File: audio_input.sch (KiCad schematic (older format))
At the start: 21 parts, among them U8 OPA1664

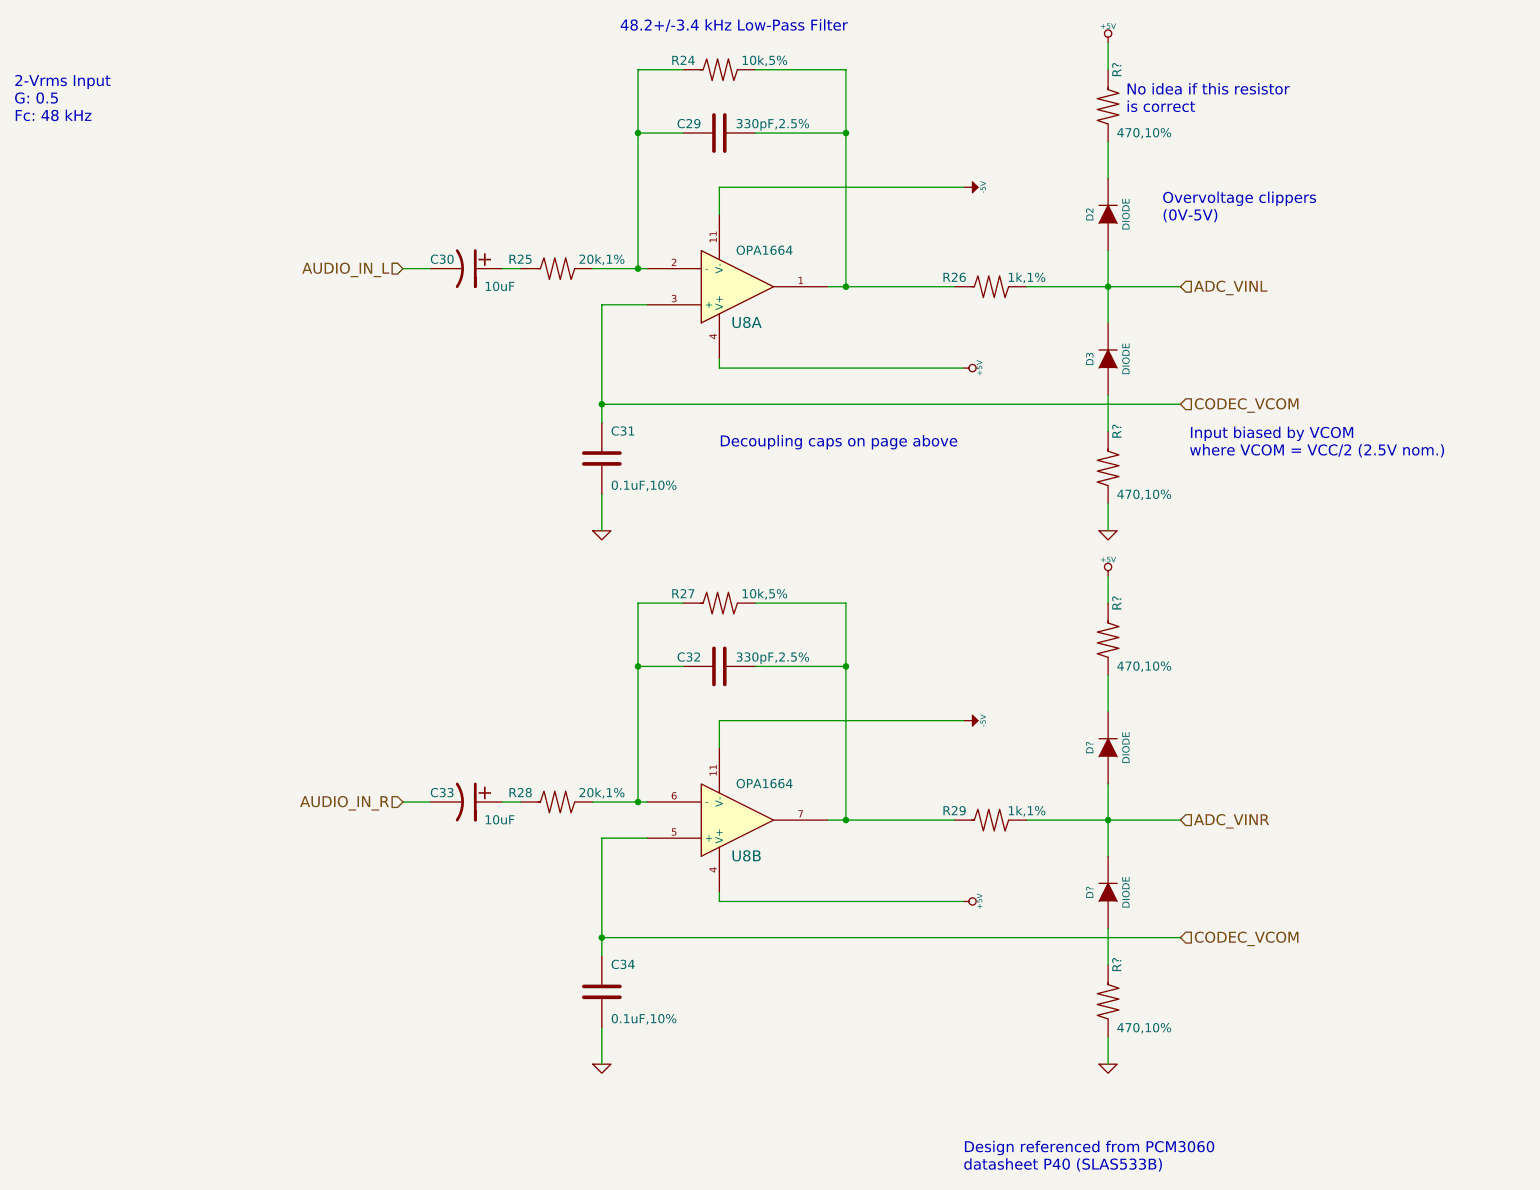
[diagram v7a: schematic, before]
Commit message: Added more footprint assoc. & eth. pulldown resistors
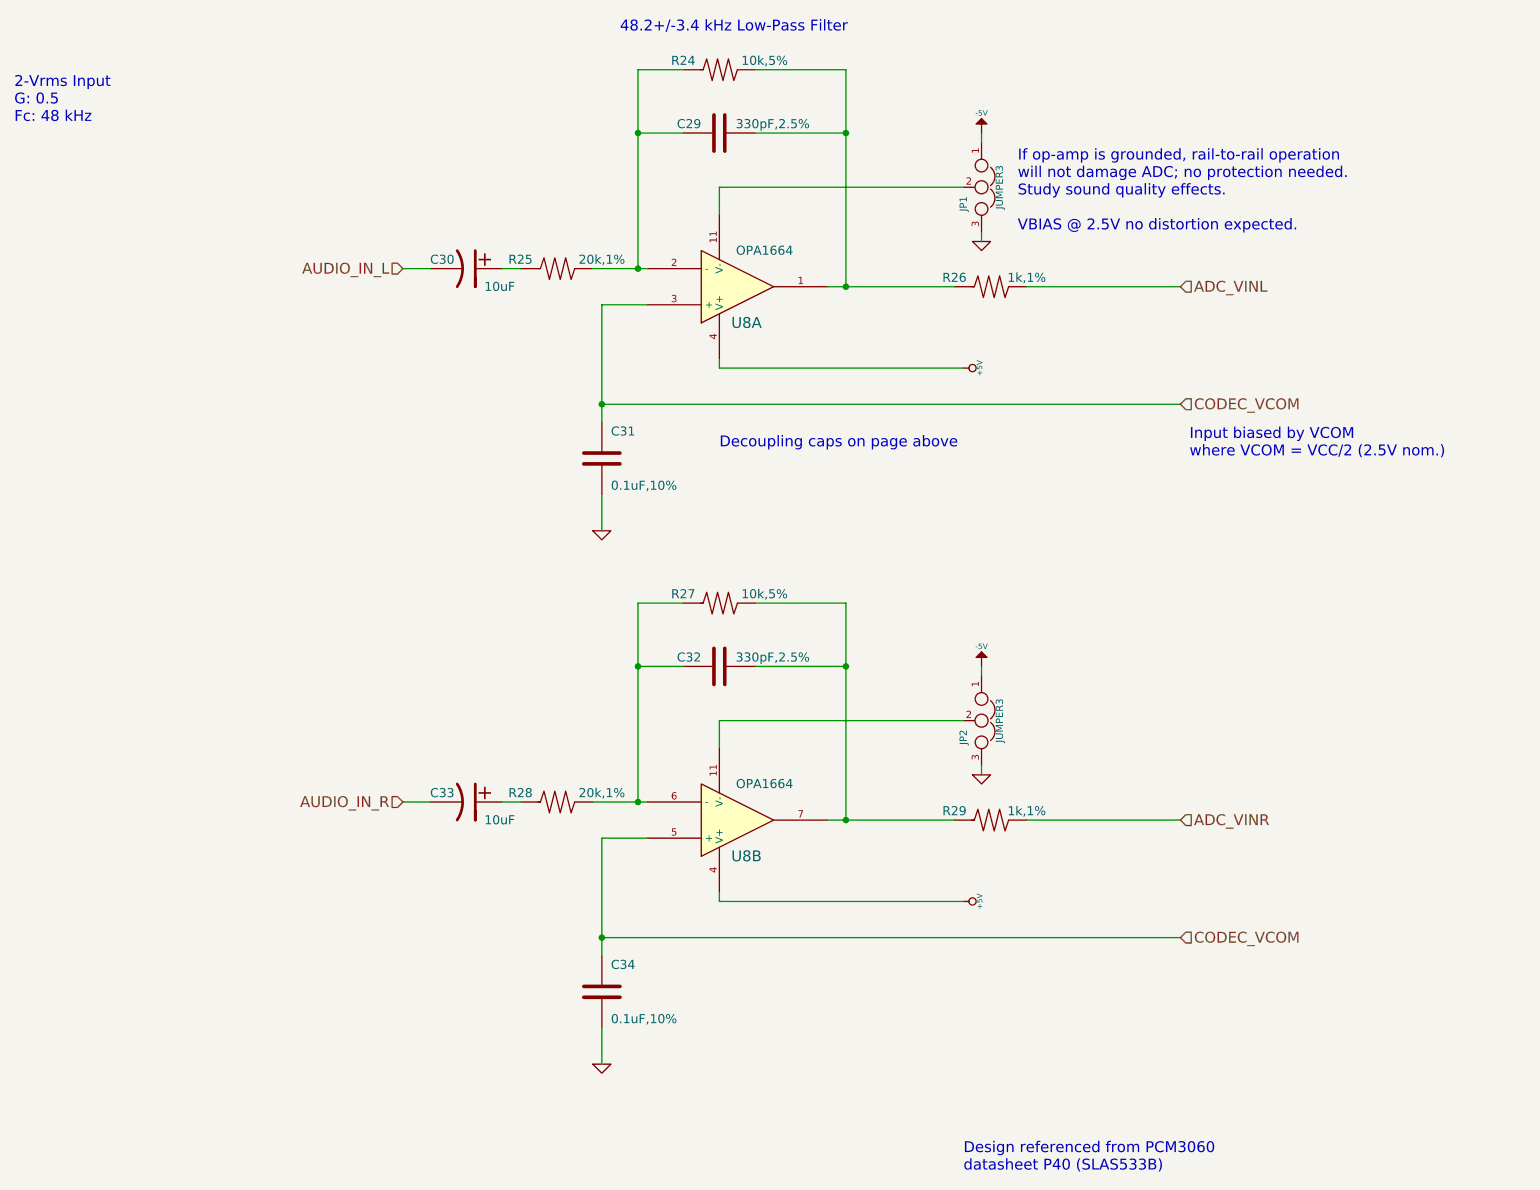
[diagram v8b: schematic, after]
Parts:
- removed D2, D3, D? (x2): DIODE, symbol DIODE
- removed R? (x4): 470,10%, symbol R
- added JP1, JP2: JUMPER3, Pin_Headers:Pin_Header_Straight_1x03, symbol JUMPER3
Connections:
- net -5V: now also JP1.1, JP2.1; no longer U8.11 (V-), U8.11 (V-)
- net GND: now also JP1.3, JP2.3
- new net: JP1.2, U8.11 (V-)
- new net: JP2.2, U8.11 (V-)
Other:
- note added: "If op-amp is grounded, rail-to-rail operation\nwill not damage ADC; no protection needed.\nStudy sound quality effects.\n\nVBIAS @ 2.5V no distortion expected."
- note removed: "No idea if this resistor\nis correct"
- note removed: "Overvoltage clippers \n(0V-5V)"
